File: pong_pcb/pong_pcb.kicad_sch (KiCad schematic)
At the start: 4 parts, among them J2 Screw_Terminal_01x02

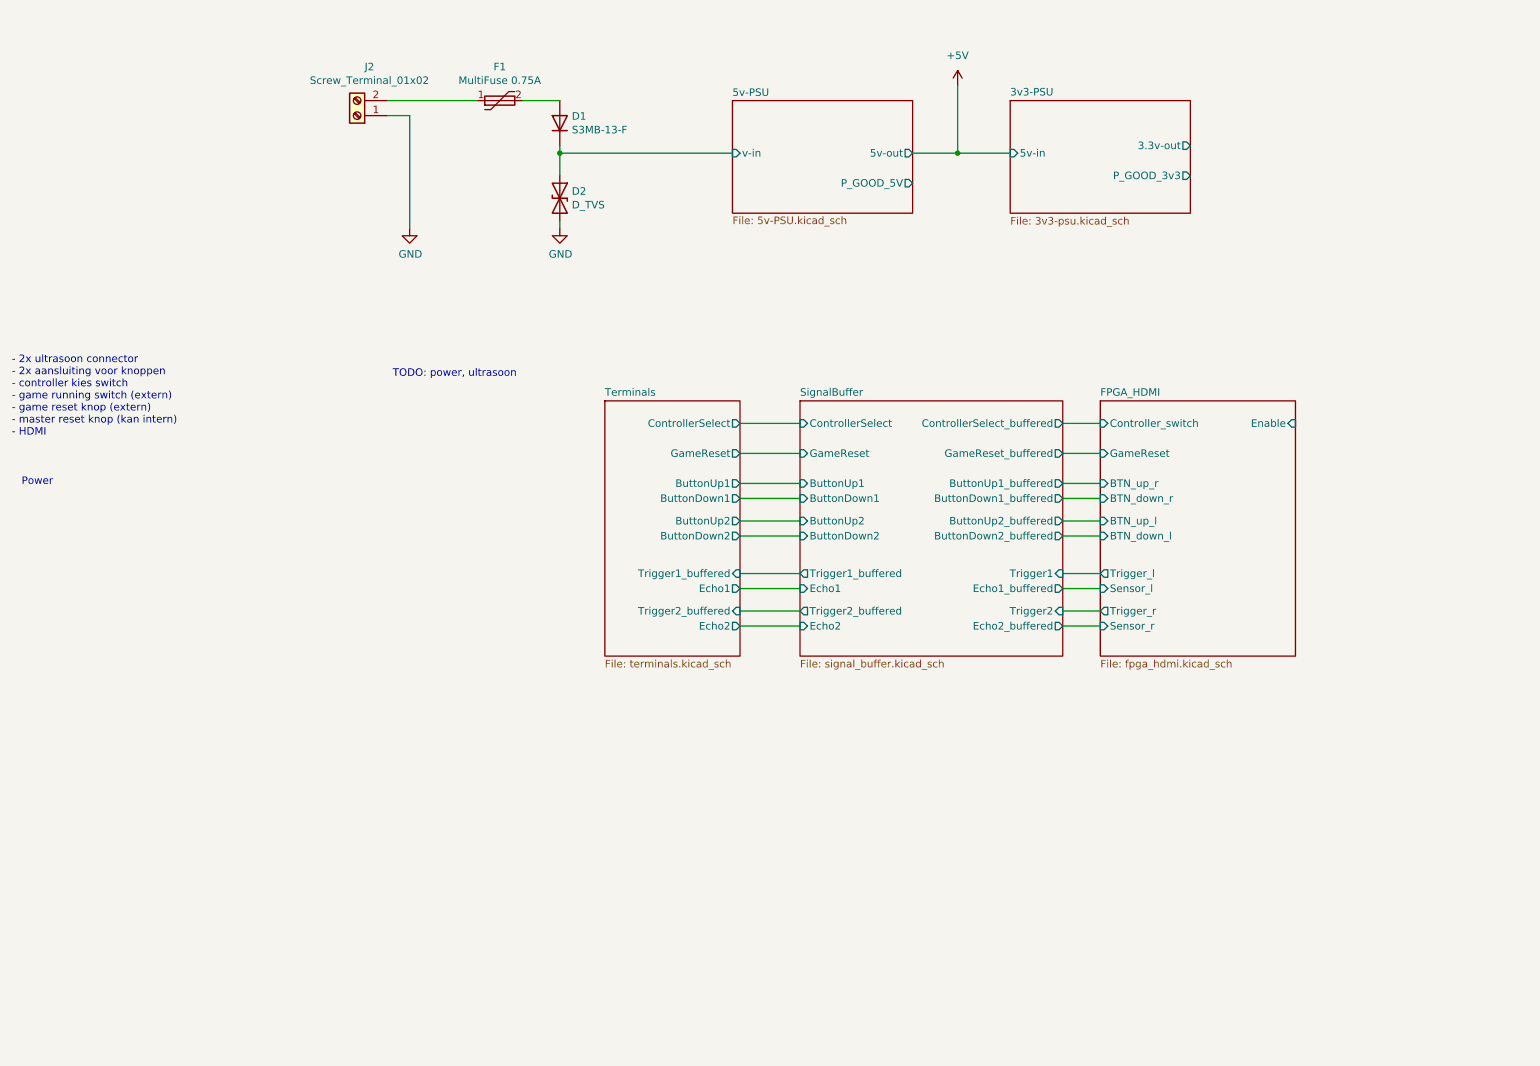
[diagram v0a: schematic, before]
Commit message: Update schema and add packages
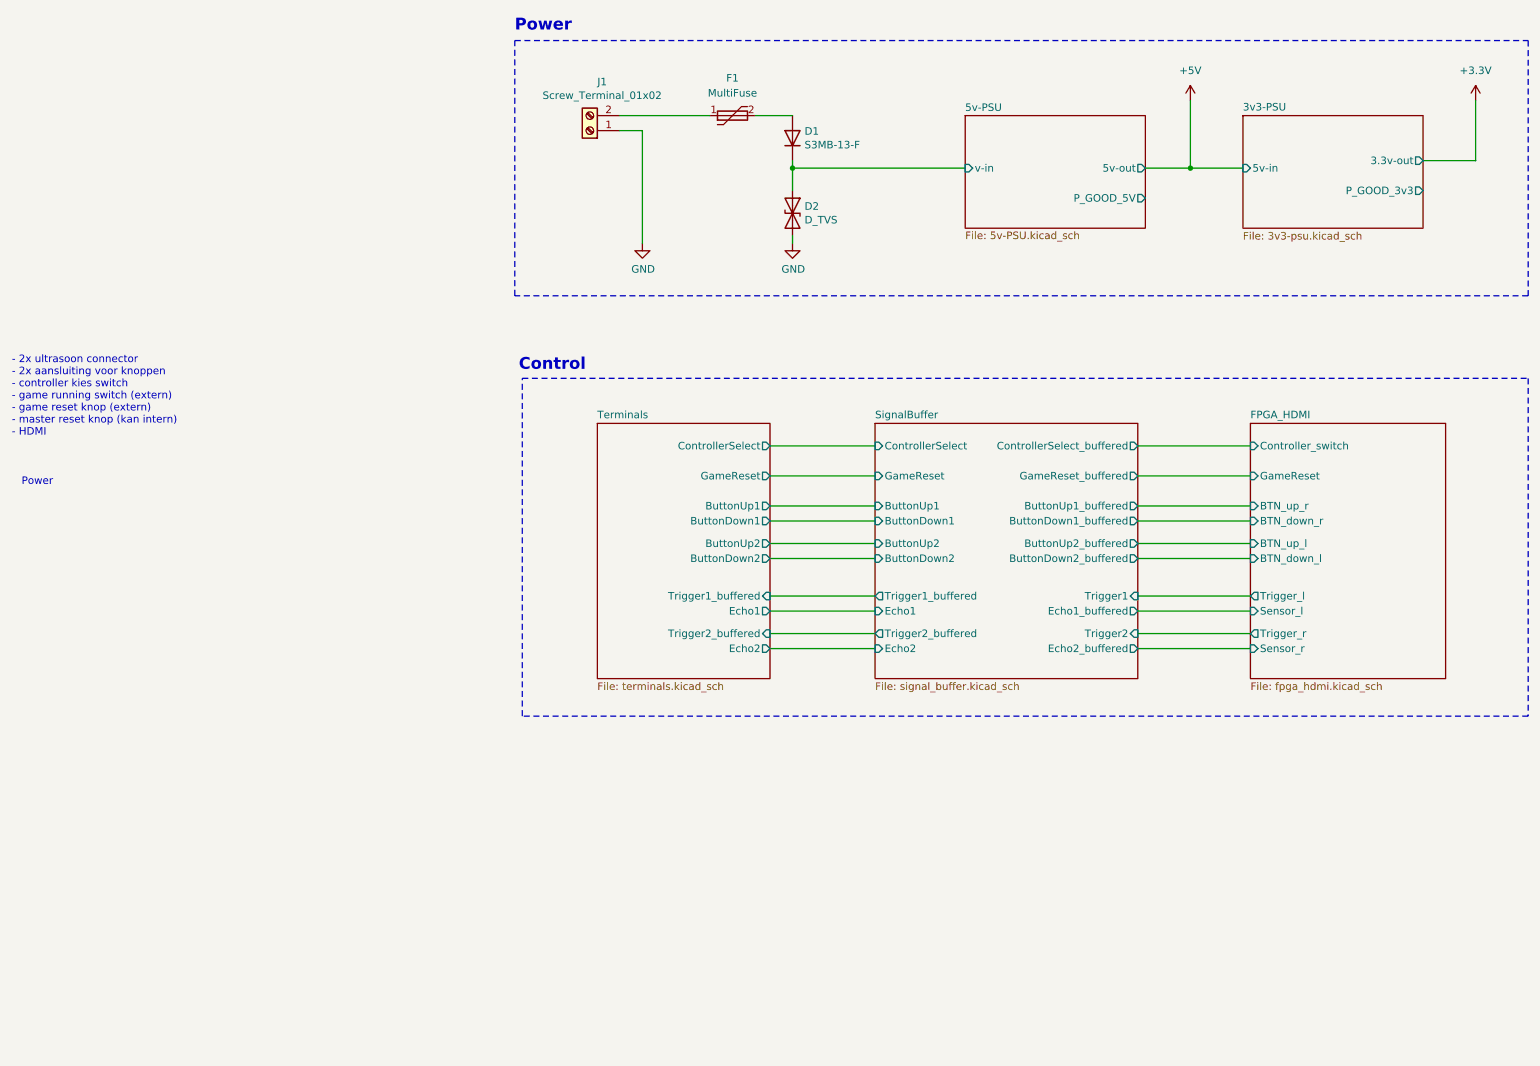
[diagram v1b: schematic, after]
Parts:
- removed F1: MultiFuse 0.75A, 3ABuck:Fuse MF-MSMF075 33X-2, symbol 3Abuck:MultiFuse
- added F1: MultiFuse, MyLib:Fuse MF-MSMF075 33X-2, symbol MyLib:MultiFuse
- renumbered J2 to J1
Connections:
- net at J1.2 (Pin_2): now also F1.1
- net at D1.2 (A): now also F1.2
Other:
- sheet FPGA_HDMI ports: added none; removed Enable
- note added: "Control"
- note removed: "TODO: power, ultrasoon"
- company: (none) -> Fontys
- moved on the sheet: D1, D2, J1

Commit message: PCB indeling maken
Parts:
- added H1, H2, H3, H4: MountingHole_Pad, MountingHole:MountingHole_3.2mm_M3_Pad_Via, symbol Mechanical:MountingHole_Pad
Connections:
- net GND: now also H1.1, H2.1, H3.1, H4.1

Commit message: Other connectors
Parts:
- J1: footprint TerminalBlock_Phoenix:TerminalBlock_Phoenix_MKDS-3-2-5.08_1x02_P5.08mm_Horizontal -> Connector_Phoenix_MSTB:PhoenixContact_MSTBA_2,5_2-G-5,08_1x02_P5.08mm_Horizontal
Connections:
- net GND: now also J1.2 (Pin_2); no longer J1.1 (Pin_1)
- net power_in: now reaches F1.1
- net power_in: now also J1.1 (Pin_1); no longer J1.2 (Pin_2)
- net power_fused: now reaches D1.2 (A), F1.2
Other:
- moved on the sheet: D1, D2, J1
